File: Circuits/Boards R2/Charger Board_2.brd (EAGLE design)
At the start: 63.5 x 50.8 mm, 71 parts, among them CON1 ISP(2X3), CON10 HEADER_3X1, CON11 HEADER_3X1, CON12 HEADER_3X1, CON13 HEADER_4X1, CON2 SCREWTERMINAL_1X2, CON3 HEADER_3X1, CON4 HEADER_3X1, CON5 HEADER_3X1, CON6 HEADER_3X1, CON7 HEADER_3X1, CON8 HEADER_3X1, CON9 HEADER_3X1, IC1 NCP1117DT33G, T1 NPN2N2222, T2 NPN2N2222, T3 SI4421DY, U1 ATMEGA324P, U2 ACS711, U3 JOYSTICKPTH

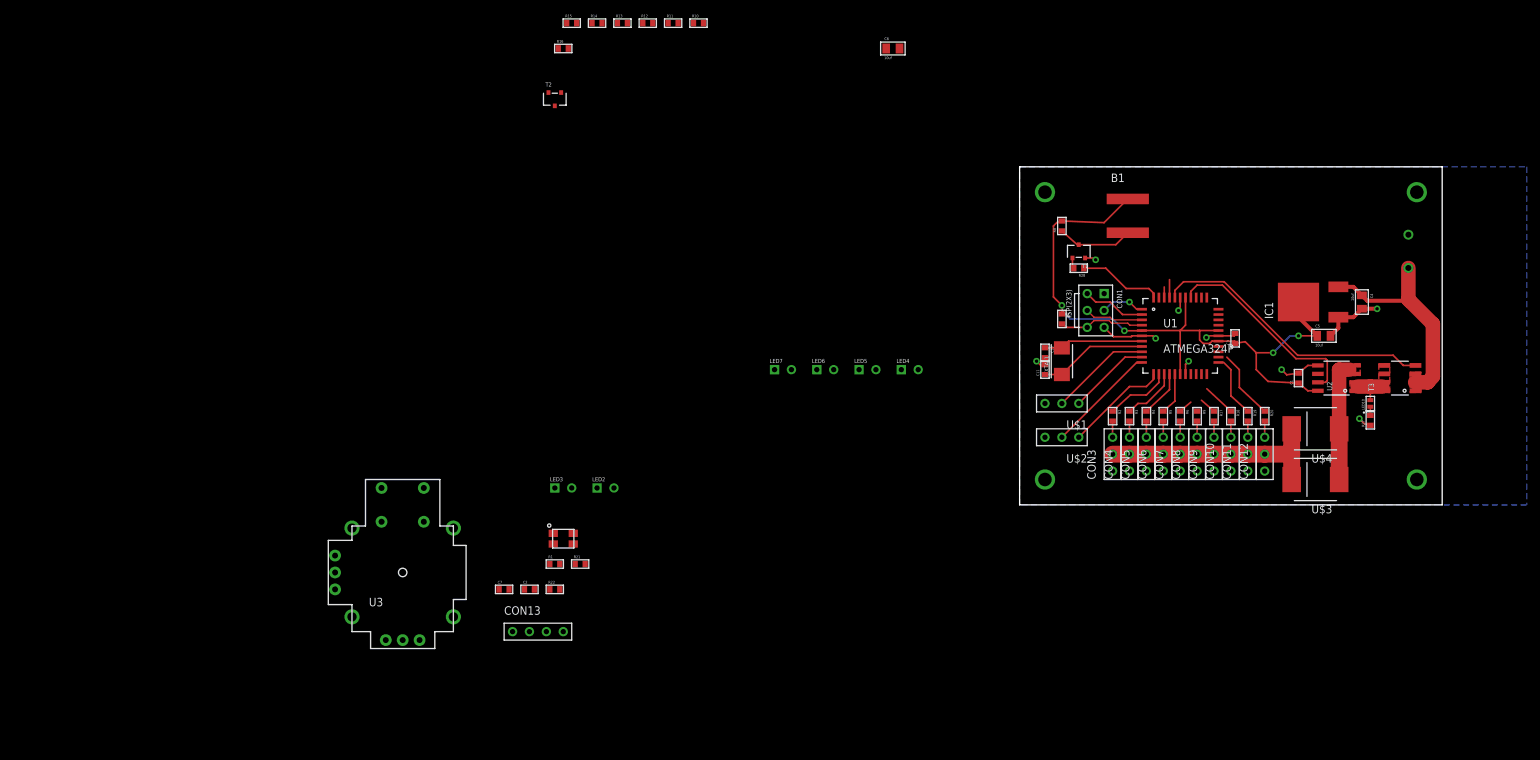
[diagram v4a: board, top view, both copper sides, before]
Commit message: 
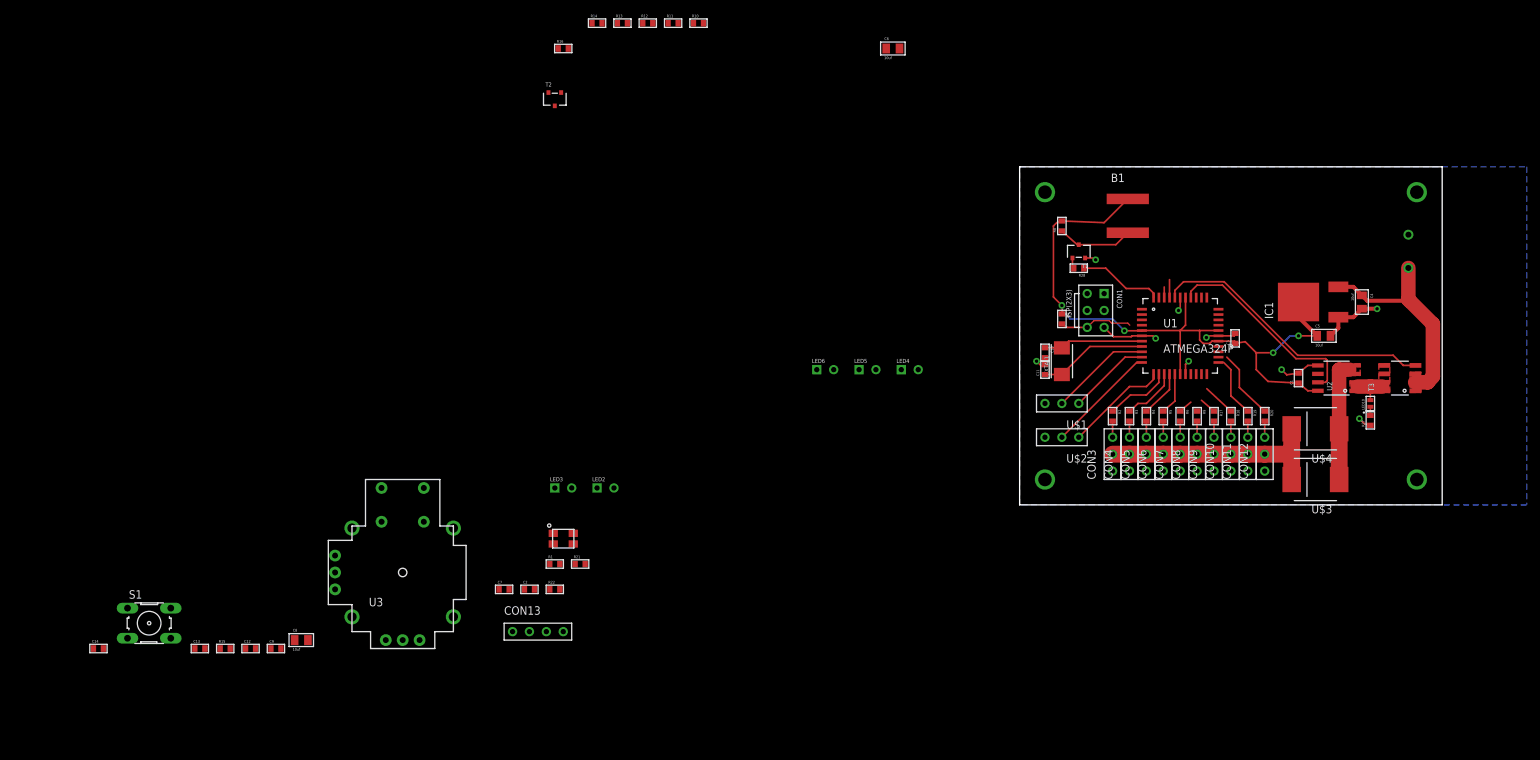
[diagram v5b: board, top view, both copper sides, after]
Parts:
- removed LED7: IR, Passive:5MM_LED_RA
- added C12, C13, C14, C9: .1uf, Passive:0603
- added C8: 10uf, Passive:0805
- added S1: (no value), switch-omron:B3F-10XX
- R10, R11, R12, R13, R14: value (none) -> 18
- R15: value (none) -> 10k
- moved R15 107.4 mm to (-119.4, -21.6)
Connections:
- net N$2 renamed MOSI
- net N$3 renamed MISO
- net N$5 renamed SCK
- removed net N$18: LED7.2, R15.2
- removed net N$6: CON1.4, R7.2, U1.4
- new net BUTTON: C13.1, R15.2, U1.34, U3.B2A
- new net HORIZONTAL: U1.35, U3.H2
- new net RESET: C14.1, CON1.4, R7.2, S1.3, S1.4, U1.4
- new net VERTICAL: U1.36, U3.V2
- net +3V3: now also U3.B1A, U3.H1, U3.V1; no longer C2.1, C6.1, C7.1, LED2.1, LED3.1, LED4.1, LED5.1, LED6.1, LED7.1
- net +5V: now also C12.1, C2.1, C6.1, C7.1, C8.1, C9.1, LED2.1, LED3.1, LED4.1, LED5.1, LED6.1
- net GND: now also C12.2, C13.2, C14.2, C8.2, C9.2, R15.1, S1.1, S1.2, U3.H3, U3.V3
- net N$10: no longer R15.1
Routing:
- net N$6: track 12.9 -> 0.00 mm
- net RESET: track 0.00 -> 11.1 mm
- net MISO: track 9.52 -> 0.00 mm
- net SCK: track 8.80 -> 0.00 mm
- net MOSI: track 6.65 -> 0.00 mm, vias 1 -> 0

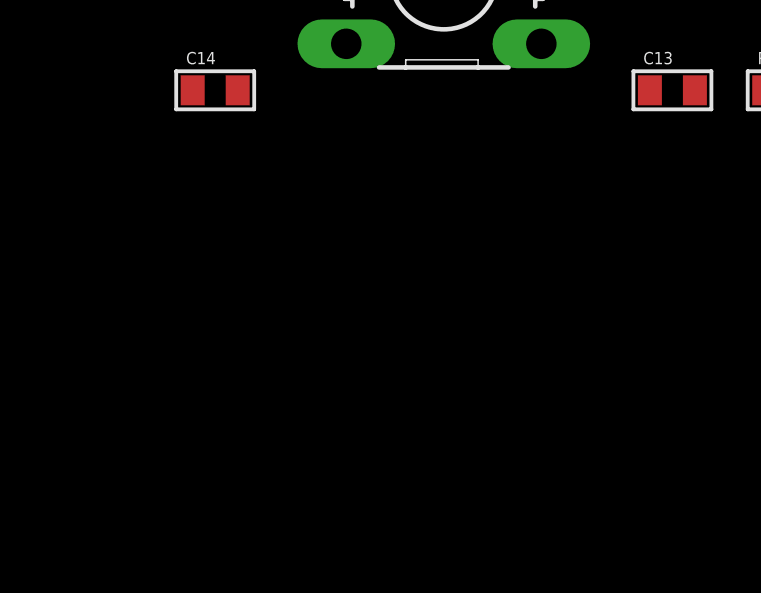
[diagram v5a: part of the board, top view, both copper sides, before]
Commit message: 
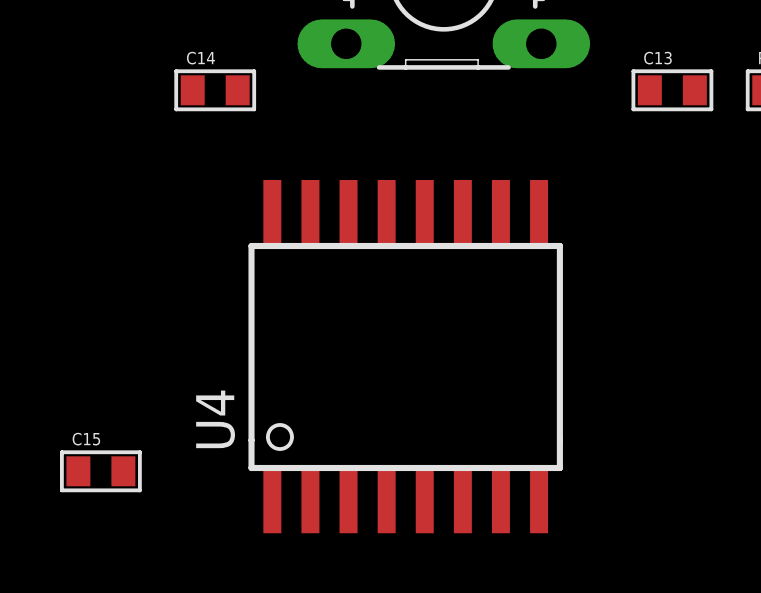
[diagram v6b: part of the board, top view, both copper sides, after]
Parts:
- added C15: .1uf, Passive:0603
- added U4: MX25L25735E, DigitalIC:SOIC16R
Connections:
- new net CS: U1.30, U4.7
- net +3V3: now also C15.1, U4.2
- net GND: now also C15.2, U4.10
- net SCK: now also U4.16
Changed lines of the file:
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@@
 </element>
 <element name="C14" library="Passive" package="0603" value=".1uf" x="-138.43" y="-21.59"/>
+<element name="U4" library="DigitalIC" package="SOIC16R" value="MX25L25735E" x="-132.08" y="-30.48"/>
+<element name="C15" library="Passive" package="0603" value=".1uf" x="-142.24" y="-34.29"/>
 </elements>
 <signals>
@@
 <contactref element="S1" pad="2"/>
 <contactref element="C14" pad="2"/>
+<contactref element="U4" pad="10"/>
+<contactref element="C15" pad="2"/>
+<wire x1="-137.68" y1="-21.59" x2="-141.49" y2="-34.29" width="0" layer="19" extent="1-1"/>
 <wire x1="-134.0612" y1="-15.5194" x2="-137.68" y2="-21.59" width="0" layer="19" extent="1-1"/>
 <wire x1="-127.5588" y1="-15.5194" x2="-134.0612" y2="-15.5194" width="0" layer="19" extent="1-1"/>
@@
 <wire x1="-111.01" y1="-21.59" x2="-114.82" y2="-21.59" width="0" layer="19" extent="1-1"/>
 <wire x1="-106.95" y1="-20.32" x2="-111.01" y2="-21.59" width="0" layer="19" extent="1-1"/>
+<wire x1="-128.905" y1="-25.68" x2="-122.44" y2="-21.59" width="0" layer="19" extent="1-1"/>
 <wire x1="-102.87" y1="-12.7" x2="-106.95" y2="-20.32" width="0" layer="19" extent="1-1"/>
 <wire x1="-90.17" y1="-20.32" x2="-102.87" y2="-12.7" width="0" layer="19" extent="1-1"/>
@@
 <contactref element="U3" pad="H1"/>
 <contactref element="U3" pad="B1A"/>
-<wire x1="-102.87" y1="-7.62" x2="-95.25" y2="-20.32" width="0" layer="19" extent="1-1"/>
+<contactref element="U4" pad="2"/>
+<contactref element="C15" pad="1"/>
+<wire x1="-135.255" y1="-35.255" x2="-142.99" y2="-34.29" width="0" layer="19" extent="1-1"/>
+<wire x1="-102.87" y1="-7.62" x2="-135.255" y2="-35.255" width="0" layer="19" extent="1-1"/>
 <wire x1="-95.885" y1="2.54" x2="-102.87" y2="-7.62" width="0" layer="19" extent="1-1"/>
+<wire x1="-95.25" y1="-20.32" x2="-102.87" y2="-7.62" width="0" layer="19" extent="1-1"/>
 <wire x1="5.08" y1="31.242" x2="-95.885" y2="2.54" width="0" layer="19" extent="1-1"/>
 <wire x1="12.7" y1="31.75" x2="13.97" y2="27.94" width="0" layer="19" extent="16-16"/>
@@
 <contactref element="CON1" pad="5"/>
 <contactref element="U1" pad="3"/>
-<wire x1="10.16" y1="29.21" x2="18.38" y2="27.8" width="0" layer="19" extent="1-1"/>
+<contactref element="U4" pad="16"/>
+<wire x1="10.16" y1="29.21" x2="-136.525" y2="-25.68" width="0" layer="19" extent="1-1"/>
+<wire x1="18.38" y1="27.8" x2="10.16" y2="29.21" width="0" layer="19" extent="1-1"/>
+</signal>
+<signal name="CS">
+<contactref element="U4" pad="7"/>
+<contactref element="U1" pad="30"/>
+<wire x1="29.88" y1="27" x2="-128.905" y2="-35.255" width="0" layer="19" extent="1-1"/>
 </signal>
 </signals>

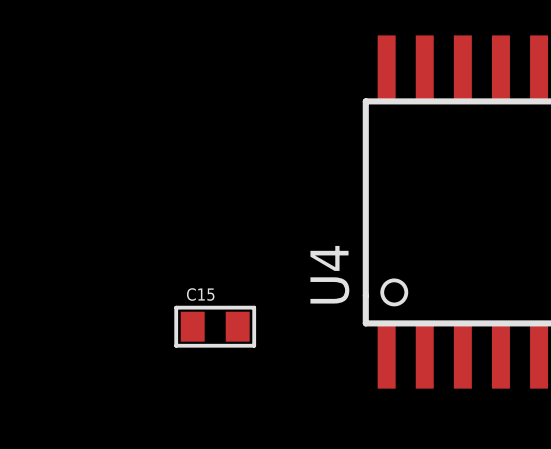
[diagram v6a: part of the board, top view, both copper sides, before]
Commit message: completed schematic for the charger board
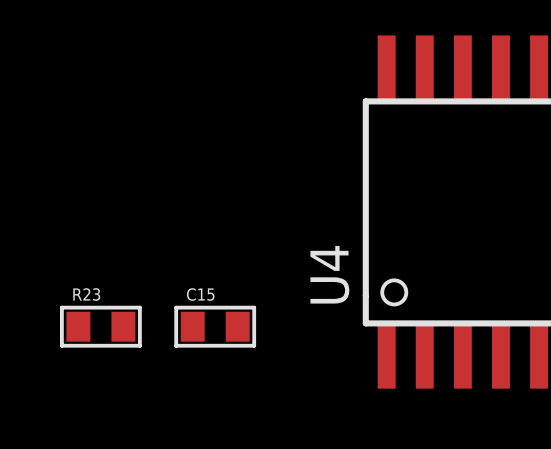
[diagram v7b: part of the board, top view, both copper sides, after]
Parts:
- added R23: 10k, Passive:0603
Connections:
- new net HOLD: U1.31, U4.1
- new net WP: U1.32, U4.9
- net +3V3: now also R23.1
- net CS: now also R23.2
- net MISO: now also U4.8
- net MOSI: now also U4.15
- net TRANSMITLEDS: now also U1.33
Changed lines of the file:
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@@
 <element name="U4" library="DigitalIC" package="SOIC16R" value="MX25L25735E" x="-132.08" y="-30.48"/>
 <element name="C15" library="Passive" package="0603" value=".1uf" x="-142.24" y="-34.29"/>
+<element name="R23" library="Passive" package="0603" value="10k" x="-146.05" y="-34.29"/>
 </elements>
 <signals>
@@
 <signal name="TRANSMITLEDS">
 <contactref element="R16" pad="1"/>
+<contactref element="U1" pad="33"/>
+<wire x1="-69.33" y1="68.58" x2="29.88" y2="29.4" width="0" layer="19" extent="1-1"/>
 </signal>
 <signal name="N$22">
@@
 <contactref element="U4" pad="2"/>
 <contactref element="C15" pad="1"/>
+<contactref element="R23" pad="1"/>
+<wire x1="-142.99" y1="-34.29" x2="-146.8" y2="-34.29" width="0" layer="19" extent="1-1"/>
 <wire x1="-135.255" y1="-35.255" x2="-142.99" y2="-34.29" width="0" layer="19" extent="1-1"/>
 <wire x1="-102.87" y1="-7.62" x2="-135.255" y2="-35.255" width="0" layer="19" extent="1-1"/>
@@
 <contactref element="CON1" pad="2"/>
 <contactref element="U1" pad="1"/>
-<wire x1="12.7" y1="29.21" x2="18.38" y2="29.4" width="0" layer="19" extent="1-1"/>
+<contactref element="U4" pad="15"/>
+<wire x1="12.7" y1="29.21" x2="-135.255" y2="-25.68" width="0" layer="19" extent="1-1"/>
+<wire x1="18.38" y1="29.4" x2="12.7" y2="29.21" width="0" layer="19" extent="1-1"/>
 </signal>
 <signal name="MISO">
 <contactref element="CON1" pad="6"/>
 <contactref element="U1" pad="2"/>
-<wire x1="10.16" y1="31.75" x2="18.38" y2="28.6" width="0" layer="19" extent="1-1"/>
+<contactref element="U4" pad="8"/>
+<wire x1="10.16" y1="31.75" x2="-127.635" y2="-35.255" width="0" layer="19" extent="1-1"/>
+<wire x1="18.38" y1="28.6" x2="10.16" y2="31.75" width="0" layer="19" extent="1-1"/>
 </signal>
 <signal name="SCK">
@@
 <contactref element="U4" pad="7"/>
 <contactref element="U1" pad="30"/>
+<contactref element="R23" pad="2"/>
+<wire x1="-128.905" y1="-35.255" x2="-145.3" y2="-34.29" width="0" layer="19" extent="1-1"/>
 <wire x1="29.88" y1="27" x2="-128.905" y2="-35.255" width="0" layer="19" extent="1-1"/>
 </signal>
+<signal name="WP">
+<contactref element="U4" pad="9"/>
+<contactref element="U1" pad="32"/>
+<wire x1="29.88" y1="28.6" x2="-127.635" y2="-25.68" width="0" layer="19" extent="1-1"/>
+</signal>
+<signal name="HOLD">
+<contactref element="U4" pad="1"/>
+<contactref element="U1" pad="31"/>
+<wire x1="29.88" y1="27.8" x2="-136.525" y2="-35.255" width="0" layer="19" extent="1-1"/>
+</signal>
 </signals>

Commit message: more board updates
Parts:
- added R24: 10k, Passive:0603
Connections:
- net +5V: now also R24.2
- net CHARGER: now also R24.1
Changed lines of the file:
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@@
 <element name="C15" library="Passive" package="0603" value=".1uf" x="-142.24" y="-34.29"/>
 <element name="R23" library="Passive" package="0603" value="10k" x="-146.05" y="-34.29"/>
+<element name="R24" library="Passive" package="0603" value="10k" x="-149.86" y="-34.29"/>
 </elements>
 <signals>
@@
 <wire x1="-18.05" y1="68.58" x2="-70.8" y2="61.96" width="0" layer="19" extent="1-1"/>
 <wire x1="9.84" y1="37.1" x2="-18.05" y2="68.58" width="0" layer="19" extent="1-1"/>
-<wire x1="12.7" y1="26.67" x2="11.43" y2="36.83" width="0" layer="19" extent="1-1"/>
-<wire x1="23.876" y1="29.21" x2="20.066" y2="25.4" width="0" layer="19" extent="1-1"/>
-<wire x1="28.321" y1="25.4" x2="24.13" y2="29.464" width="0" layer="19" extent="1-1"/>
-<wire x1="25.4" y1="21.59" x2="28.067" y2="25.146" width="0" layer="19" extent="1-1"/>
-<wire x1="39.37" y1="20.32" x2="32.25" y2="25.4" width="0" layer="19" extent="1-1"/>
-<wire x1="46.72" y1="25.4" x2="44.825" y2="20.955" width="0" layer="19" extent="1-1"/>
-<wire x1="3.81" y1="22.11" x2="12.7" y2="26.67" width="0" layer="19" extent="1-1"/>
-<wire x1="3.81" y1="15.24" x2="3.31" y2="20.82" width="0" layer="19" extent="1-1"/>
-<wire x1="3.81" y1="10.16" x2="3.81" y2="15.24" width="0" layer="19" extent="1-1"/>
-<wire x1="51.054" y1="12.954" x2="44.825" y2="20.955" width="0" layer="19" extent="1-1"/>
-<wire x1="13.97" y1="5.08" x2="3.81" y2="10.16" width="0" layer="19" extent="1-1"/>
-<wire x1="16.51" y1="5.08" x2="13.97" y2="5.08" width="0" layer="19" extent="1-1"/>
-<wire x1="19.05" y1="5.08" x2="16.51" y2="5.08" width="0" layer="19" extent="1-1"/>
-<wire x1="21.59" y1="5.08" x2="19.05" y2="5.08" width="0" layer="19" extent="1-1"/>
-<wire x1="24.13" y1="5.08" x2="21.59" y2="5.08" width="0" layer="19" extent="1-1"/>
-<wire x1="26.67" y1="5.08" x2="24.13" y2="5.08" width="0" layer="19" extent="1-1"/>
-<wire x1="29.21" y1="5.08" x2="26.67" y2="5.08" width="0" layer="19" extent="1-1"/>
-<wire x1="31.75" y1="5.08" x2="29.21" y2="5.08" width="0" layer="19" extent="1-1"/>
-<wire x1="34.29" y1="5.08" x2="31.75" y2="5.08" width="0" layer="19" extent="1-1"/>
-<wire x1="36.83" y1="5.08" x2="34.29" y2="5.08" width="0" layer="19" extent="1-1"/>
-<wire x1="58.42" y1="40.6" x2="53.705" y2="29.48" width="0" layer="19" extent="1-1"/>
 </signal>
 <signal name="RESET">
@@
 <contactref element="C9" pad="1"/>
 <contactref element="C12" pad="1"/>
+<contactref element="R24" pad="2"/>
+<wire x1="-116.32" y1="-21.59" x2="-149.11" y2="-34.29" width="0" layer="19" extent="1-1"/>
 <wire x1="-112.51" y1="-21.59" x2="-116.32" y2="-21.59" width="0" layer="19" extent="1-1"/>
 <wire x1="-108.95" y1="-20.32" x2="-112.51" y2="-21.59" width="0" layer="19" extent="1-1"/>
@@
 <wire x1="-20.05" y1="68.58" x2="-17.78" y2="20.32" width="0" layer="19" extent="1-1"/>
 <wire x1="47.9" y1="32.76" x2="-17.78" y2="20.32" width="0" layer="19" extent="1-1"/>
-<wire x1="59.49" y1="18.415" x2="59.49" y2="18.469" width="0" layer="19" extent="1-1"/>
-<wire x1="59.49" y1="17.145" x2="59.436" y2="18.415" width="0" layer="19" extent="1-1"/>
 </signal>
 <signal name="CURRENTSENSE">
@@
 <wire x1="56.134" y1="22.479" x2="57.658" y2="20.955" width="0.254" layer="1"/>
 <wire x1="57.658" y1="20.955" x2="59.49" y2="20.955" width="0.254" layer="1"/>
+<contactref element="R24" pad="1"/>
+<wire x1="23.33" y1="31.15" x2="-150.61" y2="-34.29" width="0" layer="19" extent="1-1"/>
 </signal>
 <signal name="CHARGE+">
